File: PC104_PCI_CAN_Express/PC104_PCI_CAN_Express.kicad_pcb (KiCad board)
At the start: 2 copper layers, 95.9 x 90.2 mm, 8 parts

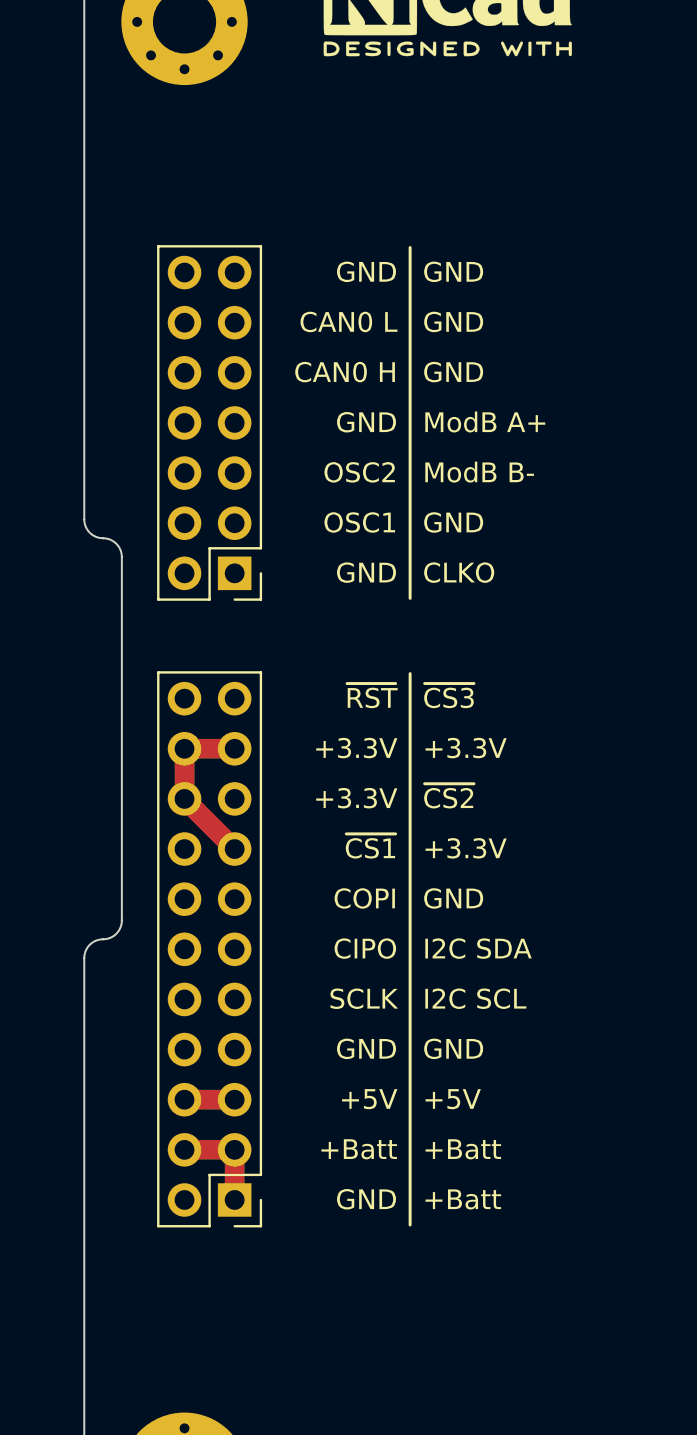
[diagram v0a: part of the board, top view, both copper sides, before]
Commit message: Adding : licence file for CC-BY-SA-4.0
Update :
- PC104_PCI_CAN_Express -> PCB silkscreen
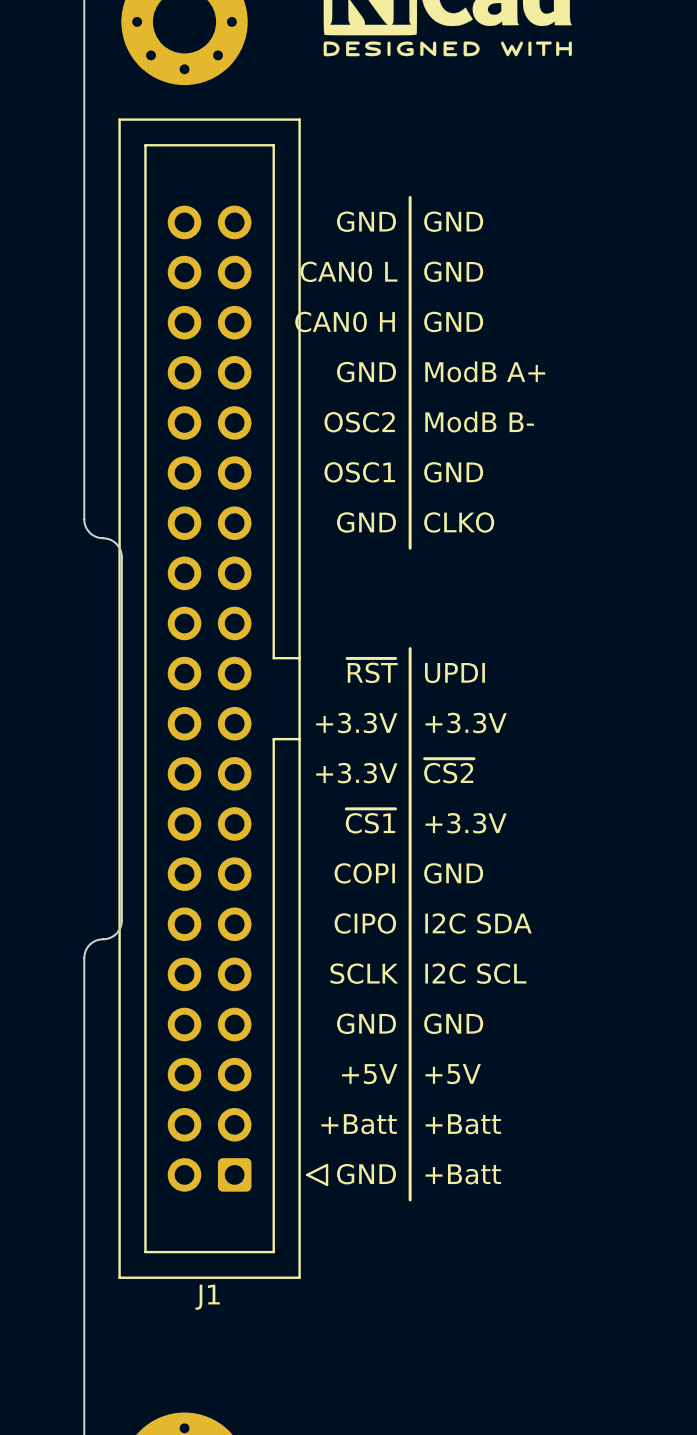
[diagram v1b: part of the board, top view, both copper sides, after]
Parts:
- removed PCIe_CAN_1: Conn_02x07_Odd_Even, Library_PCI_CAN_Express:PinHeader_2x07_P2.54mm_Vertical
- removed PCIe_SPI_1: Conn_02x11_Odd_Even, Library_PCI_CAN_Express:PinHeader_2x11_P2.54mm_Vertical
- added J1: Conn_02x20_Odd_Even, Connector_IDC:IDC-Header_2x20_P2.54mm_Vertical, F.Cu at (114.9, 110.5)
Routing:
- net +3V3: track 8.67 -> 0.00 mm
- net +BATT: track 5.08 -> 0.00 mm
- net +5V: track 2.54 -> 0.00 mm
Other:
- board text added: "UPDI"
- board text removed: "~{CS3}"

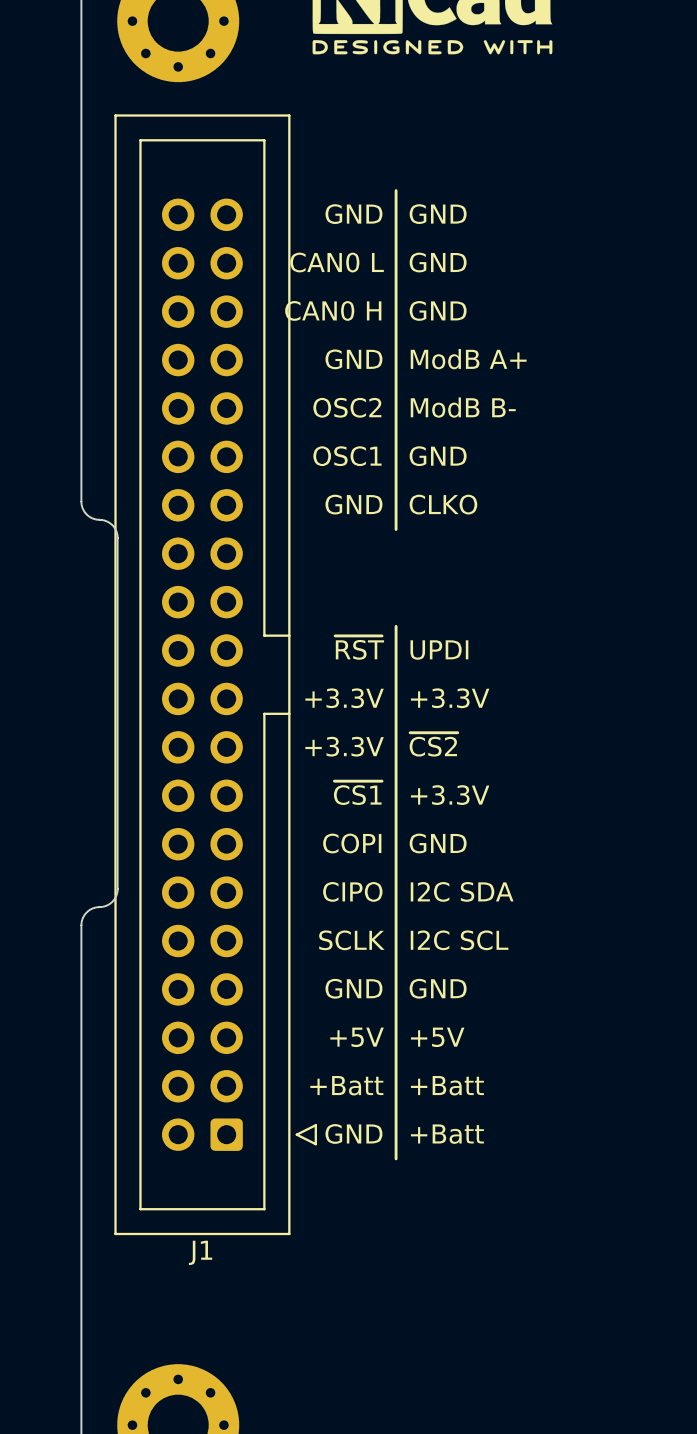
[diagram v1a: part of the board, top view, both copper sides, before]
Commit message: BUG : correction de la position du nouveau connecteur sur le PCB
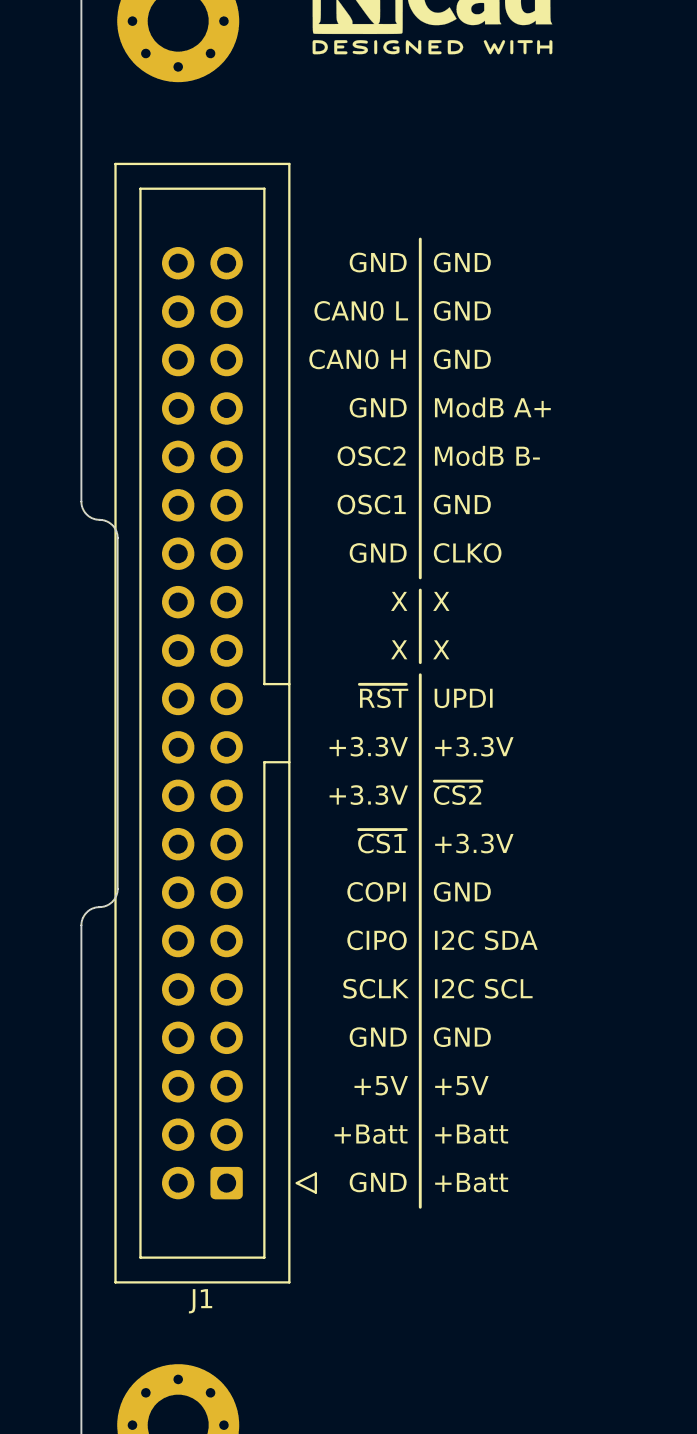
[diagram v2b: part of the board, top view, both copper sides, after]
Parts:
- moved J1 2.54 mm to (114.9, 113.0)
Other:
- board text added: "X"
